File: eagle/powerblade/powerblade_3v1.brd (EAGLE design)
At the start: 27.9 x 27.9 mm, 56 parts, among them J21 AC_INTBFILM, U1 TPS62122, U5 MAX9910, U6 MAX9910, U7 OPA2369

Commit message: updated powerfilm
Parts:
- removed CS+, TP9: TP_LONG, skyspecs:TP_LONG
- removed CS+1, RS+1, RS-1, TP6, TP7, VS+1: TP_SMD, skyspecs:TP_SMD
- removed R13: 10, rcl:R0603
- removed U5: MAX9910, powerfilm:SC70-5
- added C2: (no value), rcl:C0603
- added R2: (no value), rcl:R0603
- added U2: MCP6V3, powerfilm:SC70-5
- TP1, TP5: value TP_SMD -> TP_LONG; device skyspecs:TP_SMD -> skyspecs:TP_LONG
- moved TP5 20.4 mm to (-11.4, -35.1)
- moved TP1 9.95 mm to (-11.4, -25.9)
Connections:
- removed net N$11: C10.1, C4.1, C9.1, CS+.P$1, CS+1.P$1, L1.1, R13.1, R7.2, U1.P2
- new net N$1: R2.1, R37.2, TP4.P$1, U7.P7
- net +3V3: now also C10.1, C4.1, C9.1, L1.1, R7.2, U1.P2, U2.P5; no longer R13.2, U5.P5, VS+1.P$1
- net GND: now also C2.2, U2.P2; no longer RS-1.P$1, U5.P2
- net I_SENSE: now also C2.1, R2.2, TP1.P$1; no longer R37.2, TP4.P$1, TP7.P$1, U7.P7
- net N$38: now also U2.P1; no longer U5.P1
- net N$4: now also TP5.P$1
- net N$61: now also U2.P4; no longer TP5.P$1, U5.P4
- net N$65: now also U2.P3; no longer U5.P3
- net N$67: no longer TP6.P$1, TP9.P$1
- net VCC: no longer RS+1.P$1
- net V_SENSE: no longer TP1.P$1
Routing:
- net N$11: track 38.9 -> 0.00 mm, vias 4 -> 0
- net +3V3: track 66.5 -> 94.8 mm, vias 3 -> 7
- net I_SENSE: track 20.9 -> 0.00 mm, vias 1 -> 0
- net N$1: track 0.00 -> 16.7 mm, vias 0 -> 1
- net N$67: track 20.9 -> 15.6 mm
- net N$61: track 26.6 -> 23.8 mm
- net V_SENSE: track 27.5 -> 25.2 mm
- net N$38: track 3.13 -> 2.25 mm
- net N$65: track 2.65 -> 2.01 mm

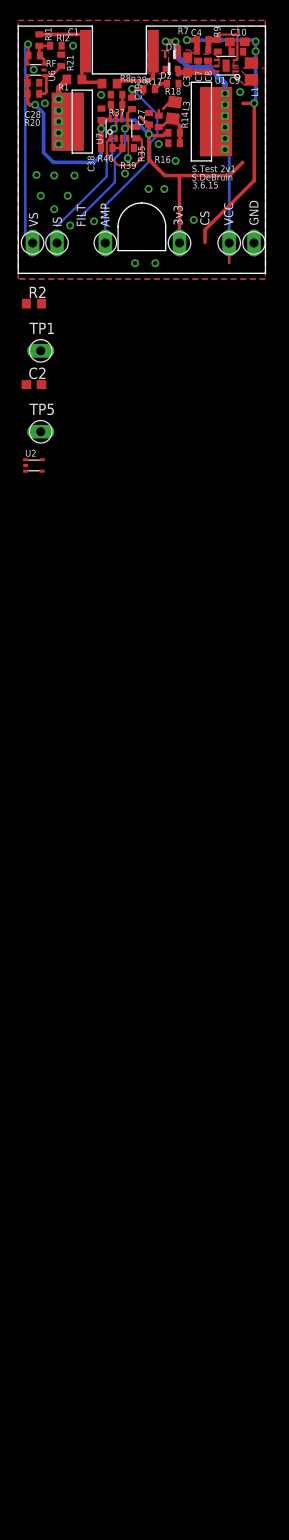
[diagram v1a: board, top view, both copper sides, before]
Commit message: updated schematic for powerblade 3v1
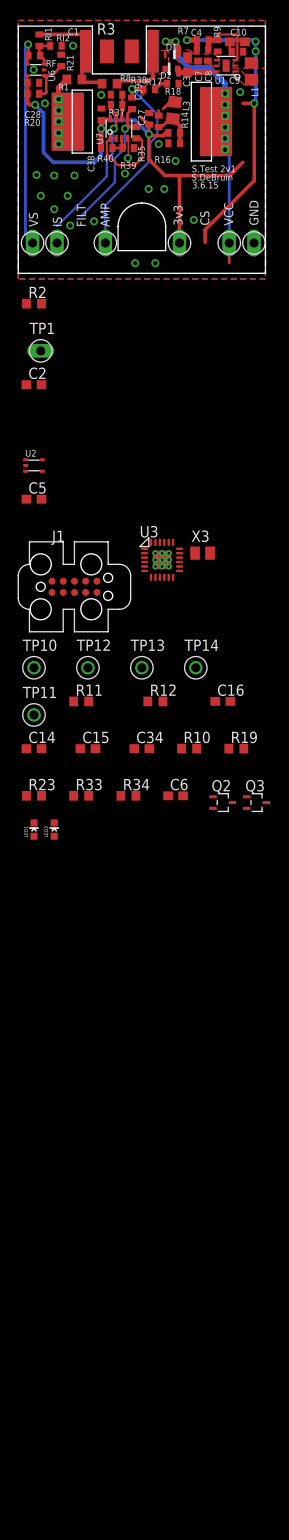
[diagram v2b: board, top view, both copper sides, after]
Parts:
- removed TP5: TP_LONG, skyspecs:TP_LONG
- added C14: 0.1uF, rcl:C0603
- added C15: 10uF, rcl:C0603
- added C16: 470nF, rcl:C0603
- added C34, C6: 8pF, rcl:C0603
- added C5: 33uF, rcl:C0603
- added J1: JTAG_14PIN_IDC, ibat:TC2050-IDC-430
- added LED1, LED2: (no value), SparkFun-LED:LED-0603
- added Q2, Q3: 2SK1829, powerfilm:SC-70-3
- added R10, R23: 120, rcl:R0603
- added R11: 134k 1%, rcl:R0603
- added R12: 67k 1%, rcl:R0603
- added R19: 47k, rcl:R0603
- added R3: (no value), rcl:R1210
- added R33, R34: NP, rcl:R0603
- added TP10, TP11, TP12, TP13, TP14: TP_STD, skyspecs:TP
- added U3: MSP430FR5738, powerfilm:VQFN-24
- added X3: 32.768kHz, general:0805
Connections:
- removed net N$4: C1.1, D1.A, D2.C, R8.2, TP5.P$1
- new net CNT0: U3.P1
- new net CNT1: U3.P2
- new net LTC_RX: R33.1, TP13.P$1, U3.P13
- new net LTC_SLEEP: U3.P15
- new net LTC_TX: R34.1, TP12.P$1, U3.P14
- new net METER_EN: U3.P17
- new net N$23: C16.2, U3.P18
- new net N$3: C34.2, U3.P22, X3.1
- new net N$49: LED1.A, R10.1
- new net N$54: LED1.C, Q2.P3
- new net N$56: C6.2, U3.P21, X3.2
- new net N$58: LED2.A, R23.1
- new net N$59: LED2.C, Q3.P3
- new net RST: J1.P10, R19.1, U3.P12
- new net RXDATA: R34.2, TP11.P$1, U3.P16
- new net TCK: J1.P7, Q2.P1, U3.P10
- new net TDI: J1.P3, Q3.P1, U3.P8
- new net TDO: J1.P1, U3.P7
- new net TEST: J1.P8, U3.P11
- new net TMS: J1.P5, U3.P9
- new net TXMOD: R33.2, TP10.P$1, U3.P3
- new net VCC_SENSE: R11.1, R12.2, U3.P4
- new net ZC: C1.1, D1.A, D2.C, R3.2, R8.2
- net +3V3: now also C14.1, C15.1, J1.P2, R10.2, R19.2, R23.2, U3.P20, U3.P24
- net GND: now also C14.2, C15.2, C16.1, C34.1, C5.2, C6.1, J1.P9, Q2.P2, Q3.P2, R12.1, TP14.P$1, U3.G1, U3.G2, U3.G3, U3.G4, U3.G5, U3.G6, U3.G7, U3.G8, U3.G9, U3.P19, U3.P23, U3.PAD
- net I_SENSE: now also U3.P6
- net VCC: now also C5.1, R11.2
- net VTEST: now also R3.1
- net V_SENSE: now also U3.P5
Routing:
- net ZC: track 0.00 -> 7.29 mm
- net N$4: track 7.29 -> 0.00 mm
- added copper zone on layer 1, net ZC
- removed copper zone on layer 1, net N$4

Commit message: finished new_final powerblade schematic
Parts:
- removed LED1: (no value), SparkFun-LED:LED-0603
- removed Q2: 2SK1829, powerfilm:SC-70-3
- removed R33, R34: NP, rcl:R0603
- removed TP10, TP11, TP12, TP13, TP14: TP_STD, skyspecs:TP
- removed TP4: TP_LONG, skyspecs:TP_LONG
- added A1: FRACTUS-2.4GHZ-FR05-S1-N-0-102, chips:FRACTUS-ANTENNA-FR05-S1-N-0-102
- added B1: BAL-NRF01D3, chips:BAL-NRF01D3
- added C11: 0.1uF, passives:0402_CAP
- added C12, C20: 1nF, passives:0402_CAP
- added C13: 4.7uF, passives:0402_CAP
- added C17: 1uF, passives:0402_CAP
- added C18, C19, C24, C25: 12pF, passives:0402_CAP
- added C21: 47nF, passives:0402_CAP
- added C22: 2.2nF, passives:0402_CAP
- added C23: 0.8pF, passives:0402_CAP
- added J4: TC2030-JLINK-NL, connector:TC2030-IDC-NL
- added L2: 15nH, passives:0402_CAP
- added L4: 10uH, passives:0603_CAP
- added Q1: 2N7002, nav:SC-70-3
- added Q4: 2SK1829, powerfilm:SC-70-3
- added R4: 12k, passives:0402_RES
- added R5, R6: 220k, rcl:R0603
- added U4: NRF51822QF, chips:QFN-48-6MM
- added X1: 16MHz, crystals:TXC-8Y
- added X2: ABS05-32.768KHZ-9-T, crystals:ABS05
- C10: value 4.7uF -> 22uF
- C7: device rcl:C0402 -> rcl:C0603
- R10: value 120 -> 220k
- moved R10 66.4 mm to (-12.2, -134.9)
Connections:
- removed net CNT0: U3.P1
- removed net CNT1: U3.P2
- removed net LTC_RX: R33.1, TP13.P$1, U3.P13
- removed net LTC_SLEEP: U3.P15
- removed net LTC_TX: R34.1, TP12.P$1, U3.P14
- removed net METER_EN: U3.P17
- removed net N$49: LED1.A, R10.1
- removed net N$54: LED1.C, Q2.P3
- removed net RXDATA: R34.2, TP11.P$1, U3.P16
- removed net TXMOD: R33.2, TP10.P$1, U3.P3
- new net A0: C24.1, U4.45, X2.A
- new net A1: C25.1, U4.46, X2.B
- new net AVDD: C12.1, C17.1, L2.1, U4.35, U4.36
- new net BLE_ENABLE: Q1.P1, R5.1, U3.P15
- new net BLE_LPINT: U3.P16, U4.3
- new net DCC: L4.2, U4.2
- new net FROMBLE_RX: U3.P14, U4.48
- new net GND2: B1.GND, C11.2, C12.2, C13.2, C17.2, C18.2, C19.2, C20.2, C21.2, C22.2, C23.2, C24.2, C25.2, J4.5, Q1.P3, R4.2, U4.13, U4.33, U4.34, U4.GND
- new net GND3: C2.2, C27.2, C28.2, C38.2, Q4.P3, R16.1, R18.1, R21.1, R38.1, R39.1, RI2.1, U2.P2, U6.P2, U7.P4
- new net METER_ENABLE: Q4.P1, R6.1, U3.P17
- new net N$14: L2.2, L4.1
- new net N$16: C18.1, U4.37, X1.1
- new net N$17: C19.1, U4.38, X1.3
- new net N$18: C20.1, U4.39
- new net N$19: C21.1, U4.29
- new net N$4: A1.1, B1.SE, C23.1
- new net N$5: B1.ANT1, U4.31
- new net N$6: B1.ANT2, U4.32
- new net SWDCLK: J4.4, R4.1, U4.24
- new net SWDIO/!RESET: J4.2, U4.23
- new net TOBLE_TX: U3.P13, U4.47
- new net VDD_PA: B1.VCC, C22.1, U4.30
- net +3V3: now also C11.1, C13.1, J4.1, U4.1, U4.12; no longer R10.2
- net GND: now also Q1.P2, Q4.P2, R10.2, R5.2, R6.2; no longer C2.2, C27.2, C28.2, C38.2, Q2.P2, R16.1, R18.1, R21.1, R38.1, R39.1, RI2.1, TP14.P$1, U2.P2, U6.P2, U7.P4
- net N$1: no longer TP4.P$1
- net TCK: no longer Q2.P1
- net TDI: now also R10.1
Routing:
- net GND: track 8.61 -> 6.25 mm

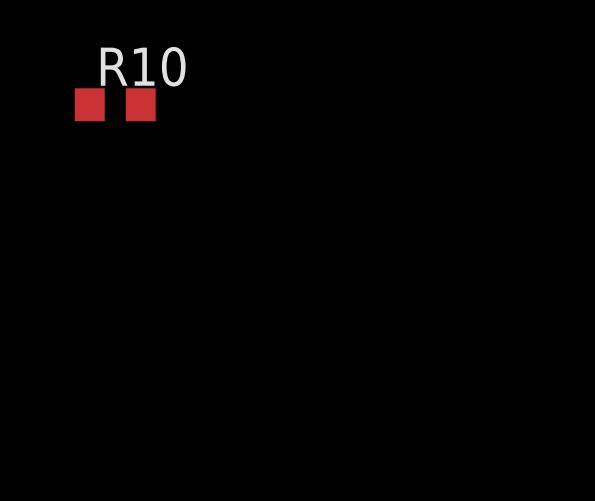
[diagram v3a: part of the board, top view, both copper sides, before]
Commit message: added zc voltage divider to powerblade_3v1 schematic
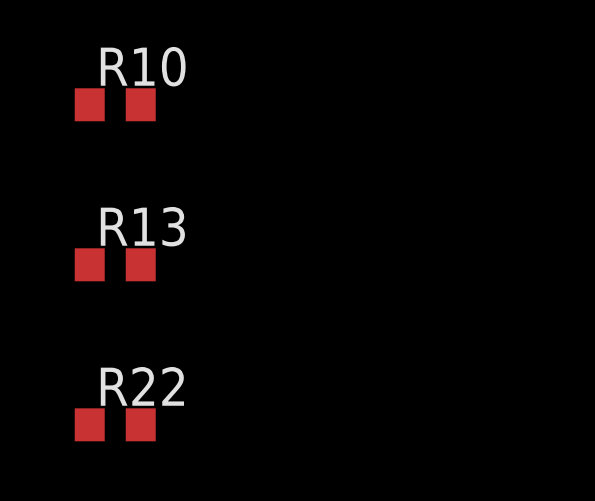
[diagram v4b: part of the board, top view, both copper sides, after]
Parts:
- added R13: 67k 1%, rcl:R0603
- added R22: 134k 1%, rcl:R0603
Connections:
- new net N$8: R13.2, R22.1, U3.P3
- net GND: now also R13.1
- net ZC: now also R22.2
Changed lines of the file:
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@@
 <element name="R6" library="rcl" package="R0603" value="220k" x="-12.192" y="-129.54"/>
 <element name="R10" library="rcl" package="R0603" value="220k" x="-12.192" y="-134.874"/>
+<element name="R13" library="rcl" package="R0603" value="67k 1%" x="-12.192" y="-140.208">
+<attribute name="DIGIKEY" value="P66.5KHCT-ND" x="-12.192" y="-140.208" size="1.778" layer="27" display="off"/>
+</element>
+<element name="R22" library="rcl" package="R0603" value="134k 1%" x="-12.192" y="-145.542">
+<attribute name="DIGIKEY" value="P133KHCT-ND" x="-12.192" y="-145.542" size="1.778" layer="27" display="off"/>
+</element>
 </elements>
 <signals>
@@
 <contactref element="Q4" pad="P2"/>
 <contactref element="R10" pad="2"/>
+<contactref element="R13" pad="1"/>
+<wire x1="-11.342" y1="-134.874" x2="-13.042" y2="-140.208" width="0" layer="19" extent="1-1"/>
 <wire x1="-11.342" y1="-129.54" x2="-11.342" y2="-134.874" width="0" layer="19" extent="1-1"/>
 <wire x1="-13.292" y1="-126.38" x2="-11.342" y2="-129.54" width="0" layer="19" extent="1-1"/>
@@
 <wire x1="0.79375" y1="4.60375" x2="1.27" y2="5.08" width="0.4064" layer="1"/>
 <contactref element="R3" pad="2"/>
-<wire x1="1.28" y1="7.9629" x2="2.63375" y2="7.5565" width="0" layer="19" extent="1-1"/>
+<contactref element="R22" pad="2"/>
+<wire x1="-2.80125" y1="4.28625" x2="-11.342" y2="-145.542" width="0" layer="19" extent="1-1"/>
+<wire x1="2.63375" y1="7.5565" x2="1.28" y2="7.9629" width="0" layer="19" extent="1-1"/>
 <wire x1="2.63375" y1="5.969" x2="2.63375" y2="7.5565" width="0" layer="19" extent="1-1"/>
 <wire x1="-1.14" y1="7.9375" x2="1.28" y2="7.9629" width="0" layer="19" extent="1-1"/>
@@
 <wire x1="4.261" y1="-49.28" x2="-12.906" y2="-85.468" width="0" layer="19" extent="1-1"/>
 </signal>
+<signal name="N$8">
+<contactref element="U3" pad="P3"/>
+<contactref element="R22" pad="1"/>
+<contactref element="R13" pad="2"/>
+<wire x1="-11.342" y1="-140.208" x2="-13.042" y2="-145.542" width="0" layer="19" extent="1-1"/>
+<wire x1="0.311" y1="-49.28" x2="-11.342" y2="-140.208" width="0" layer="19" extent="1-1"/>
+</signal>
 </signals>

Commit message: finished parts for first page
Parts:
- C3, C5: value 33uF -> 22uF
- R3: value (none) -> 80k
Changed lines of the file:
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@@
 </element>
 <element name="D1" library="powerfilm" package="BZT52" value="ZENERBZT52" x="3.33375" y="7.5565" smashed="yes">
-<attribute name="DIGIKEY_2" value="BZT52C15T-7DICT-ND " x="37.62375" y="-36.8935" size="1.778" layer="27" display="off"/>
 <attribute name="DIGIKEY" value="BZT52C10T-7DICT-ND " x="37.62375" y="-36.8935" size="1.778" layer="27" display="off"/>
 <attribute name="NAME" x="2.69875" y="8.03275" size="0.762" layer="25"/>
@@
 <attribute name="NAME" x="2.06375" y="4.85775" size="0.762" layer="25"/>
 </element>
-<element name="C3" library="rcl" package="C0603" value="33uF" x="5.16255" y="6.44525" smashed="yes" rot="R270">
-<attribute name="DIGIKEY" value="718-1672-1-ND" x="-39.28745" y="-36.73475" size="1.778" layer="27" rot="R270" display="off"/>
+<element name="C3" library="rcl" package="C0603" value="22uF" x="5.16255" y="6.44525" smashed="yes" rot="R270">
+<attribute name="DIGIKEY" value="445-9077-1-ND" x="-39.28745" y="-36.73475" size="1.778" layer="27" rot="R270" display="off"/>
 <attribute name="NAME" x="4.6863" y="5.17525" size="0.762" layer="25" rot="R270"/>
 </element>
@@
 <element name="C10" library="rcl" package="C0603" value="22uF" x="10.795" y="9.017" smashed="yes" rot="R180">
 <attribute name="NAME" x="10.00125" y="9.72185" size="0.762" layer="25"/>
+<attribute name="DIGIKEY" value="445-9077-1-ND" x="10.795" y="9.017" size="1.778" layer="27" rot="R180" display="off"/>
 </element>
 <element name="VS+" library="skyspecs" package="TP_LONG" value="TP_LONG" x="4.2545" y="-13.716" smashed="yes" rot="R90">
@@
 <attribute name="DIGIKEY" value="MCP6V31UT-E/LTCT-ND" x="-12.192" y="-38.862" size="1.778" layer="27" display="off"/>
 </element>
-<element name="R3" library="rcl" package="R1210" value="" x="-2.54" y="7.9375"/>
-<element name="C5" library="rcl" package="C0603" value="33uF" x="-12.192" y="-42.672">
-<attribute name="DIGIKEY" value="718-1672-1-ND" x="-12.192" y="-42.672" size="1.778" layer="27" display="off"/>
+<element name="R3" library="rcl" package="R1210" value="80k" x="-2.54" y="7.9375">
+<attribute name="DIGIKEY" value="P80.6KAACT-ND" x="-2.54" y="7.9375" size="1.778" layer="27" display="off"/>
+<attribute name="DIGIKEY_2" value="P69.8KAACT-ND" x="-2.54" y="7.9375" size="1.778" layer="27" display="off"/>
+<attribute name="DIGIKEY_3" value="P40.2KAACT-ND" x="-2.54" y="7.9375" size="1.778" layer="27" display="off"/>
+</element>
+<element name="C5" library="rcl" package="C0603" value="22uF" x="-12.192" y="-42.672">
+<attribute name="DIGIKEY" value="445-9077-1-ND" x="-12.192" y="-42.672" size="1.778" layer="27" display="off"/>
 </element>
 <element name="U3" library="powerfilm" package="VQFN-24" value="MSP430FR5738" x="2.286" y="-49.53">
